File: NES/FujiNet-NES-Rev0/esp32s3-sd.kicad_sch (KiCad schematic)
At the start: 14 parts, among them J2 microSD, SW3 S3_RST, SW4 S3_BOOT, U9 ESP32-S3-WROOM-1-N16R8

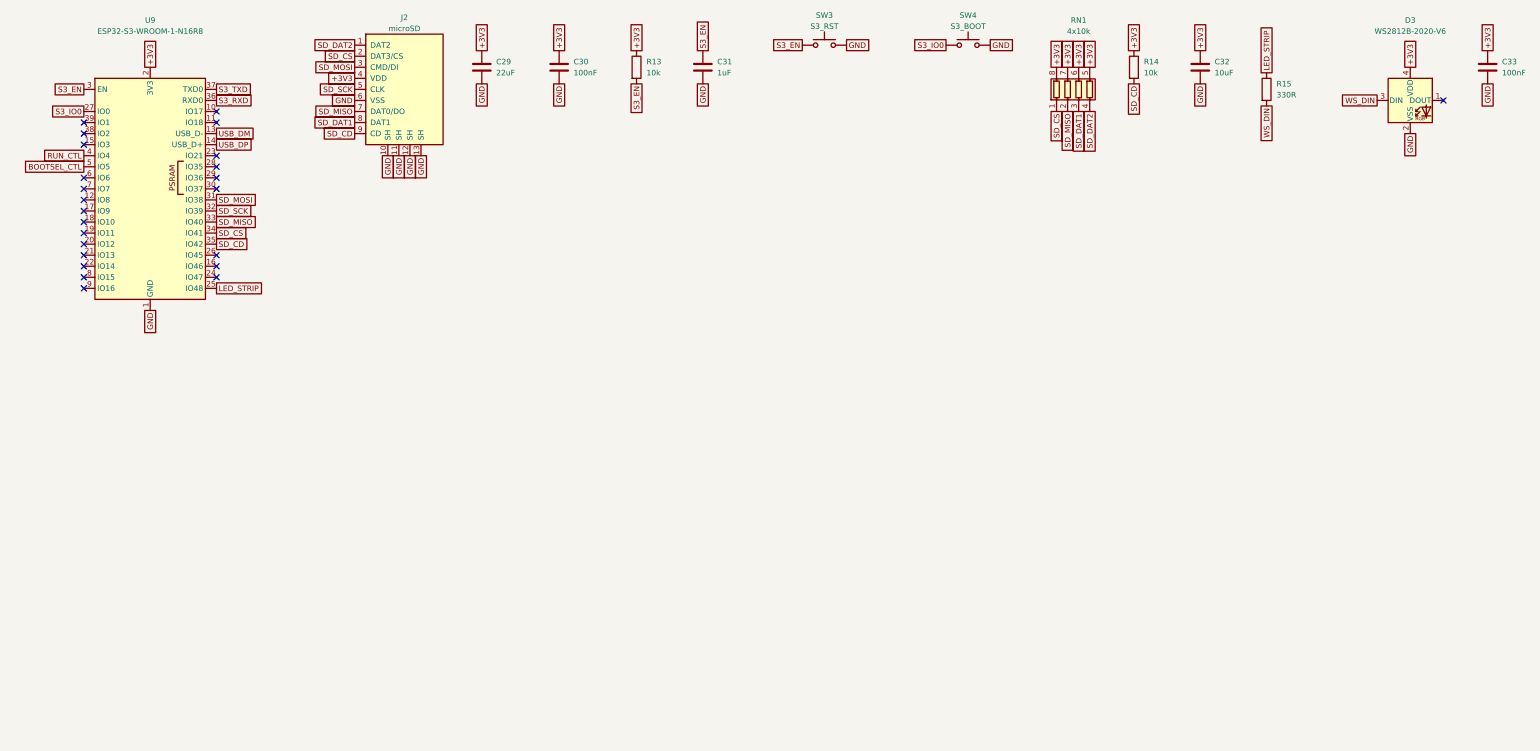
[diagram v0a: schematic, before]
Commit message: Nes rev0 (#48)
* NES: add the FujiNet-NES-Rev0 schematic

RP2354B on the 5 V cart bus with two AS6C4008-55 SRAMs (PRG, CHR) whose
bank lines come from the RP's PIO, 74HCT595/253/14/00/32 glue, and the
Astrocade Rev0 ESP32-S3, USB-UART and power sheets carried over.
Generated from tools/design.py the same way as Astrocade/rev0; ERC
reports no violations and tools/check_nets.py checks every GPIO, SRAM
line and decode equation against fujinet-firmware's nes_cart.h and
fujiversal-nes.h.

Schematic only: no layout, no board built, nothing run on a console.
The edge pinout follows the nesdev Cartridge connector page (pin 37 is
SYSTEM CLK, 2.50 mm pitch).

Co-Authored-By: Claude Fable 5.1 <noreply@anthropic.com>

* NES Rev0: audit the schematic with kicad-happy and redo it

Datasheet-backed review of the first Rev0 schematic (kicad-happy analyzer,
ngspice, 28 deep-review findings all evidence-gated, 453 netlist checks
against fujinet-firmware nes-bringup) and the fixes it called for:

- edge footprint was mirrored (pin 1 west); nesdev and two measured
  NES-EWROM-01 references put pin 1 east on the label side. Fingers are now
  2.0 x 12 mm (ends 3.0 at +/-44.25), 2.50 pitch, copper 1.0-13.0 mm in,
  Nintendo's front/back mask depths
- RP2350 pads are 5 V-tolerant only while IOVDD is powered: the IOVDD group
  moves to an AP2112K (20 us) rail +3V3_RP; VREG_VIN stays on the buck
- 74HCT595 /OE = NAND(PWR_OK, POR) with 100k pull-downs on every bit, so
  the register cannot enable the SRAMs before the RP loads it or while
  the console is off
- PRG /WE = NAND4(M2, ROMSEL, !R/W, PRG_WE_EN) on a CD74HCT20, one gate
  after M2 (was three after the console's /ROMSEL decoder vs ~30 ns hold)
- CIRAM /CE through the 74HCT253's second half, tri-stated by PWR_OK_N
- console 5 V through an AO3401A P-FET (gate = VBUS) instead of a Schottky
- console-sense divider 22k/100k (TI 74HCT14 VT+ reaches 0.70 x VCC)
- WS2812B-2020 on +5V (datasheet VDD 3.7-5.3 V, VIH 2.7 V)
- VBUS decoupling at t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
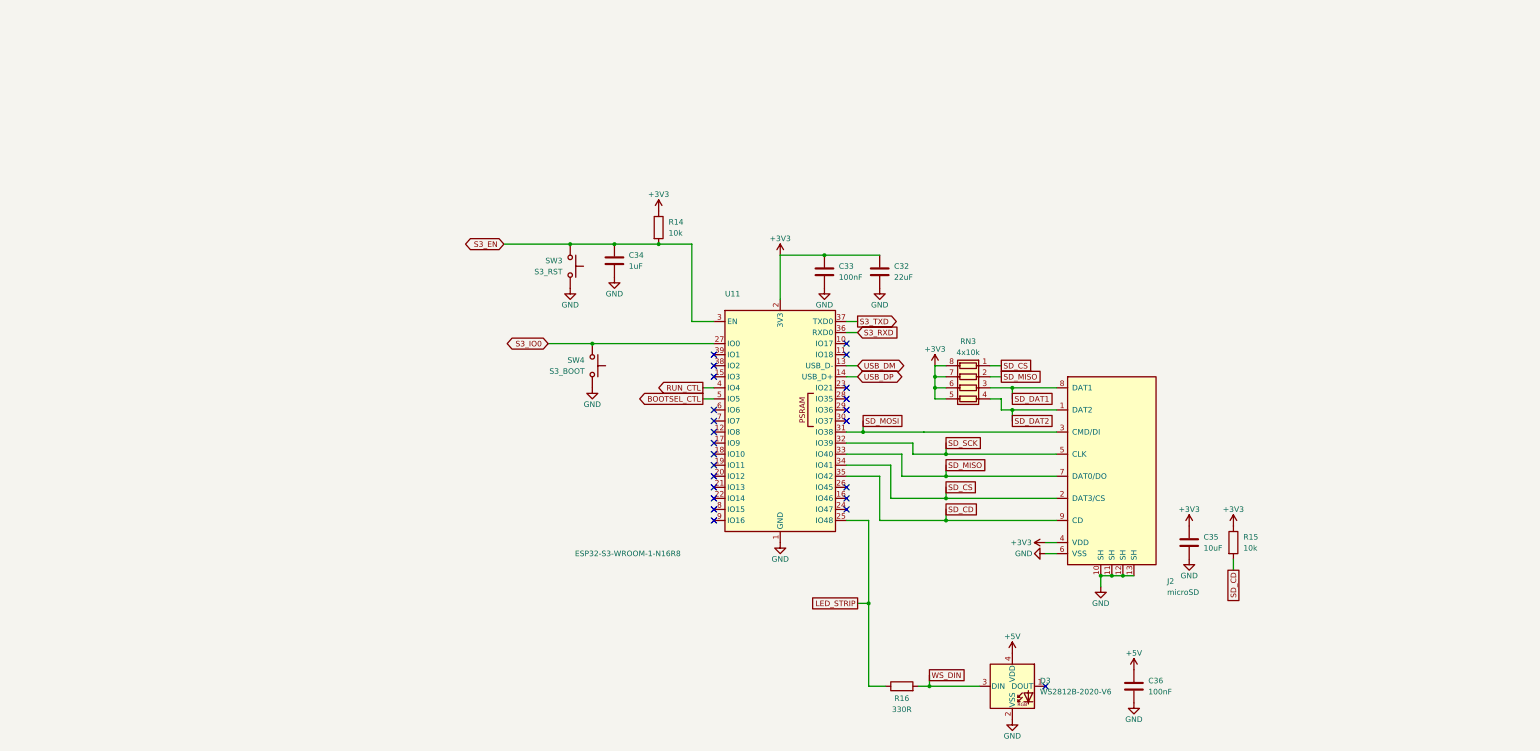
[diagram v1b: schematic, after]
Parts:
- removed C29: 22uF, FujiNet-NES:C_0805_2012Metric, symbol Device:C
- removed C30: 100nF, FujiNet-NES:C_0603_1608Metric, symbol Device:C
- removed C31: 1uF, FujiNet-NES:C_0603_1608Metric, symbol Device:C
- removed R13: 10k, FujiNet-NES:R_0603_1608Metric, symbol Device:R
- removed RN1: 4x10k, FujiNet-NES:R_Array_Convex_4x0603, symbol Device:R_Pack04
- removed U9: ESP32-S3-WROOM-1-N16R8, FujiNet-NES:ESP32-S3-WROOM-1, symbol RF_Module:ESP32-S3-WROOM-1
- added C34: 1uF, FujiNet-NES:C_0603_1608Metric, symbol Device:C
- added C35: 10uF, FujiNet-NES:C_0603_1608Metric, symbol Device:C
- added C36: 100nF, FujiNet-NES:C_0603_1608Metric, symbol Device:C
- added R16: 330R, FujiNet-NES:R_0603_1608Metric, symbol Device:R
- added RN3: 4x10k, FujiNet-NES:R_Array_Convex_4x0603, symbol Device:R_Pack04
- added U11: ESP32-S3-WROOM-1-N16R8, FujiNet-NES:ESP32-S3-WROOM-1, symbol RF_Module:ESP32-S3-WROOM-1
- C32: value 10uF -> 22uF; footprint FujiNet-NES:C_0603_1608Metric -> FujiNet-NES:C_0805_2012Metric; LCSC C19702 -> C45783; MPN CL10A106KP8NNNC -> CL21A226MAQNNNE
- R15: value 330R -> 10k; LCSC C23138 -> C25804; MPN 0603WAF3300T5E -> 0603WAF1002T5E
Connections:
- net +3V3: now also R15.1, C35.1, RN3.5 (R4.2), RN3.6 (R3.2), RN3.7 (R2.2), RN3.8 (R1.2), U11.2 (3V3); no longer D3.4 (VDD)
- net BOOTSEL_CTL: now also U11.5 (IO5)
- net GND: now also C34.2, C35.2, C36.2, U11.1 (GND), U11.40 (GND), U11.41 (GND)
- net LED_STRIP: now also R16.1, U11.25 (IO48); no longer R15.1
- net RUN_CTL: now also U11.4 (IO4)
- net S3_EN: now also R14.2, C34.1, U11.3 (EN)
- net S3_IO0: now also U11.27 (IO0)
- net S3_RXD: now also U11.36 (RXD0)
- net S3_TXD: now also U11.37 (TXD0)
- net SD_CD: now also R15.2, U11.35 (IO42); no longer R14.2
- net SD_CS: now also RN3.1 (R1.1), U11.34 (IO41)
- net SD_DAT1: now also RN3.3 (R3.1)
- net SD_DAT2: now also RN3.4 (R4.1)
- net SD_MISO: now also RN3.2 (R2.1), U11.33 (IO40)
- net SD_MOSI: now also U11.31 (IO38)
- net SD_SCK: now also U11.32 (IO39)
- net USB_DM: now also U11.13 (USB_D-)
- net USB_DP: now also U11.14 (USB_D+)
- net WS_DIN: now also R16.2; no longer R15.2
- new net +5V: C36.1, D3.4 (VDD)
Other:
- title: FujiNet NES Rev0 - ESP32-S3 FujiNet core, microSD, status LED -> FujiNet NES Rev0 - ESP32-S3, microSD, status LED
- moved on the sheet: C32, C33, D3, J2, R14, R15, SW3, SW4
